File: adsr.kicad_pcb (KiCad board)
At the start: 2 copper layers, 30 x 242.9 mm, 70 parts, among them J1 AudioJack2_SwitchT, J2 AudioJack2_SwitchT, J3 AudioJack2_SwitchT, J4 Conn_02x05_Odd_Even, Q1 BC547, Q2 BC547, Q3 BC547, Q4 BS170, SW1 SW_Push, SW2 SW_DPDT_x2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

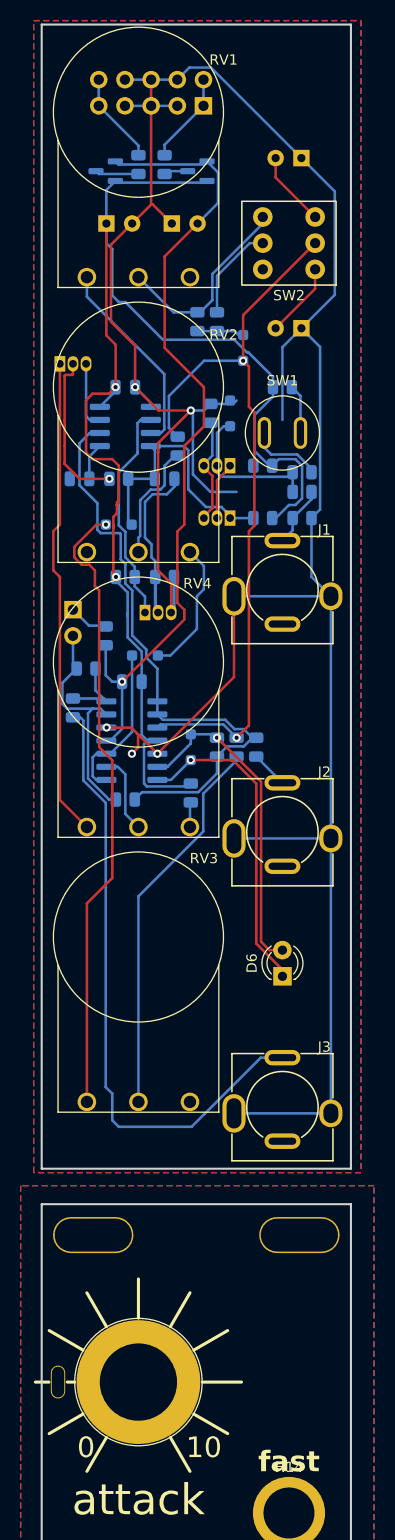
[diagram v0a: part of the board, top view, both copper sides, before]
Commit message: slightly more compact pcb
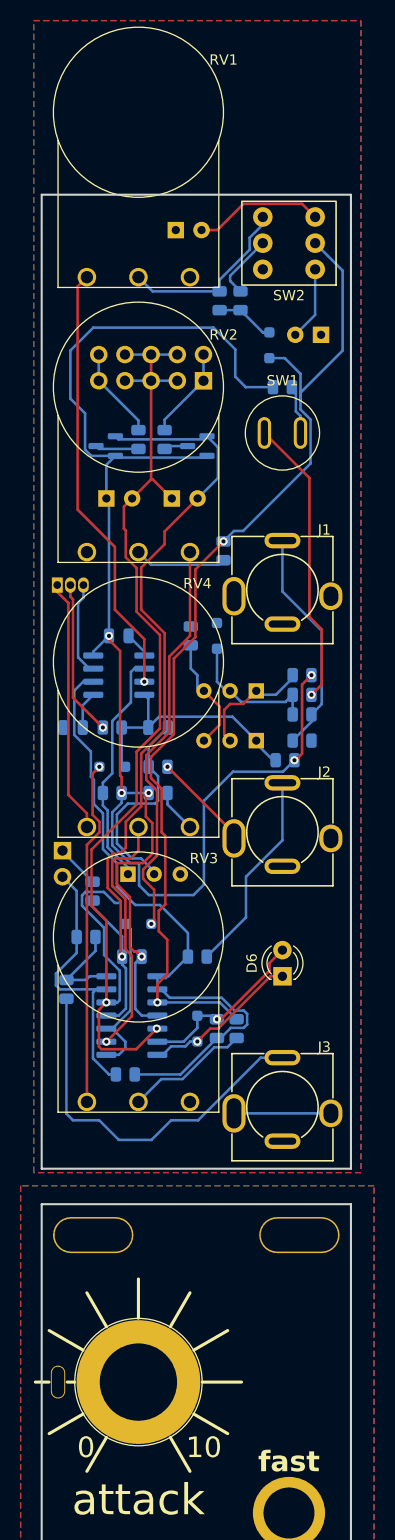
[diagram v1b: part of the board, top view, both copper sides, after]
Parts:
- Q1, Q2, Q3: footprint Package_TO_SOT_THT:TO-92_Inline -> Package_TO_SOT_THT:TO-92L_Inline_Wide
- moved D5 27.3 mm to (56.5, 114.3)
- moved R22 27.3 mm to (43.8, 110.5)
- moved R13 27.3 mm to (60.3, 114.3)
- moved R18 27.3 mm to (58.4, 114.3)
- moved C1 26.7 mm to (47.7, 62.9)
- moved C2 26.7 mm to (54.0, 62.9)
- moved C7 26.7 mm to (50.2, 107.3)
- moved R19 26.7 mm to (49.5, 118.7)
- moved U2 26.7 mm to (50.2, 113.0)
- moved D7 26.7 mm to (56.5, 57.8)
- moved D8 26.7 mm to (47.6, 57.8)
- moved J4 26.7 mm to (57.1, 51.4)
- moved R1 26.7 mm to (53.3, 57.1)
- moved R2 26.7 mm to (50.8, 57.1)
- moved D4 26.0 mm to (50.8, 104.1)
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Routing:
- net GND: track 275.9 -> 132.7 mm, vias 5 -> 3
- net +12V: track 130.3 -> 159.4 mm, vias 2 -> 6
- net Net-(D2-A): track 60.8 -> 33.6 mm
- net Net-(D3-K): track 73.3 -> 99.9 mm
- net /DECAY_CW: track 13.2 -> 39.4 mm, vias 0 -> 1
- net /RELEASE: track 37.4 -> 12.1 mm
- net /INV: track 60.6 -> 36.5 mm
- net Net-(U1-Q): track 19.3 -> 42.3 mm, vias 0 -> 1
- net Net-(Q4-D): track 46.5 -> 24.7 mm
- net Net-(R4-Pad1): track 7.18 -> 28.1 mm, vias 0 -> 1
- net /SUSTAIN: track 7.78 -> 24.6 mm, vias 0 -> 1
- net /OUT: track 3.59 -> 19.9 mm
- net Net-(J1-PadT): track 5.89 -> 22.2 mm
- net Net-(D5-A): track 31.1 -> 15.3 mm
- net Net-(D5-K): track 31.7 -> 17.2 mm
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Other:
- board size 30 x 242.9 mm -> 30 x 226.4 mm

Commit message: prepped for manu
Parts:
- moved H1 18.4 mm to (48.1, 132.5)
- moved H3 18.4 mm to (48.1, 255.0)
- moved H2 18.4 mm to (28.1, 132.5)
- moved H4 18.4 mm to (28.1, 255.0)
- moved H10 18.4 mm to (46.5, 178.2)
- moved H11 18.4 mm to (46.5, 216.9)
- moved H12 18.4 mm to (46.5, 243.6)
- moved H13 18.4 mm to (46.5, 229.6)
- moved H14 18.4 mm to (47.1, 159.8)
- moved H5 18.4 mm to (32.5, 147.1)
- moved H6 18.4 mm to (32.5, 173.7)
- moved H7 18.4 mm to (32.5, 200.4)
- moved H8 18.4 mm to (32.5, 227.1)
- moved H9 18.4 mm to (46.5, 193.4)
- moved C1 18.3 mm to (29.4, 62.7)
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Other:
- board size 30 x 226.4 mm -> 30 x 224.8 mm

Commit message: v2 fixes
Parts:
- H13: footprint Eurorack:Mech-LED-Hole-4mm -> Eurorack:Mech-LED-Hole-3mm-Bezel
- moved C4 2.50 mm to (38.6, 36.6), turned to 180 degrees
- moved C8 2.45 mm to (47.8, 46.8), turned to 0 degrees
- turned D4 to 180 degrees
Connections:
- C4 pad 1: GND -> Net-(SW2B-C)
- C4 pad 2: Net-(SW2B-C) -> GND
- C8 pad 1: GND -> Net-(SW2B-A)
- C8 pad 2: Net-(SW2B-A) -> GND
- D4 pad 2: /DECAY_CW -> Net-(D4-A)
- RV2 pad 1: unconnected-(RV2-Pad1) -> Net-(D4-A)
- RV2 pad 3: /DECAY_CW -> unconnected-(RV2-Pad3)
- U2 pad 10: Net-(D4-K) -> /SUSTAIN
- U2 pad 9: /SUSTAIN -> Net-(D4-K)
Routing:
- net Net-(D4-A): track 0.00 -> 39.9 mm, vias 0 -> 1
- net /DECAY_CW: track 39.4 -> 0.00 mm, vias 1 -> 0
- net +12V: track 159.4 -> 157.0 mm
- net Net-(D4-K): track 16.2 -> 15.1 mm
- net -12V: track 81.3 -> 82.2 mm
- net Net-(U1-THR): track 62.7 -> 63.6 mm
- net GND: track 132.7 -> 133.5 mm
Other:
- board text added: "thismatters/adsr/v2"
- board text removed: "thismatters/adsr/v1"

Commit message: new design language, adding pcb to readme
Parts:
- C1, C2: value 22u 35V -> 22u 50V
- C8: value 1u 35V Tant -> 1u 50V Tant
- H11, H12: footprint Eurorack:Mech-AudioJack-Hole-Output -> Eurorack:Mech-AudioJack-Hole-Output-CV
- H9: footprint Eurorack:Mech-AudioJack-Hole -> Eurorack:Mech-AudioJack-Hole-Input-Gate
